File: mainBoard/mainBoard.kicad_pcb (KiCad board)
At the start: 4 copper layers, 50 x 60 mm, 46 parts, among them J1 Conn_01x04, J10 Conn_02x07_Odd_Even, J2 Conn_01x04, J3 Conn_01x03, J6 Conn_01x07, J7 Conn_01x07, J8 Conn_01x02, M1 Conn_01x01, M2 Conn_01x01, U1 MAX15062A, U2 STM32H503CBT6, U3 DRV8251ADDAR

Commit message: Popisky
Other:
- board text added: "CURRENT_SENS"
- board text added: "SERVIO_PSB V 1.0"
- board text removed: "PROUD"
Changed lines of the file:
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@@
     (effects (font (size 1.5 1.5) (thickness 0.2)) (justify left bottom mirror))
   )
-  (gr_text "PROUD" (at 135 92.5) (layer "B.SilkS")
+  (gr_text "CURRENT_SENS" (at 133.45 92.5) (layer "B.SilkS")
     (effects (font (size 1.5 1.5) (thickness 0.2)) (justify bottom mirror))
   )
@@
     (effects (font (size 1.5 1.5) (thickness 0.2)) (justify bottom))
   )
-  (gr_text "PROUD" (at 135 92.5) (layer "F.SilkS")
+  (gr_text "SERVIO_PSB V 1.0" (at 170.875 93.75 90) (layer "F.SilkS")
+    (effects (font (size 1.5 1.5) (thickness 0.3) bold) (justify left bottom))
+  )
+  (gr_text "CURRENT_SENS" (at 133.45 92.5) (layer "F.SilkS")
     (effects (font (size 1.5 1.5) (thickness 0.2)) (justify bottom))
   )

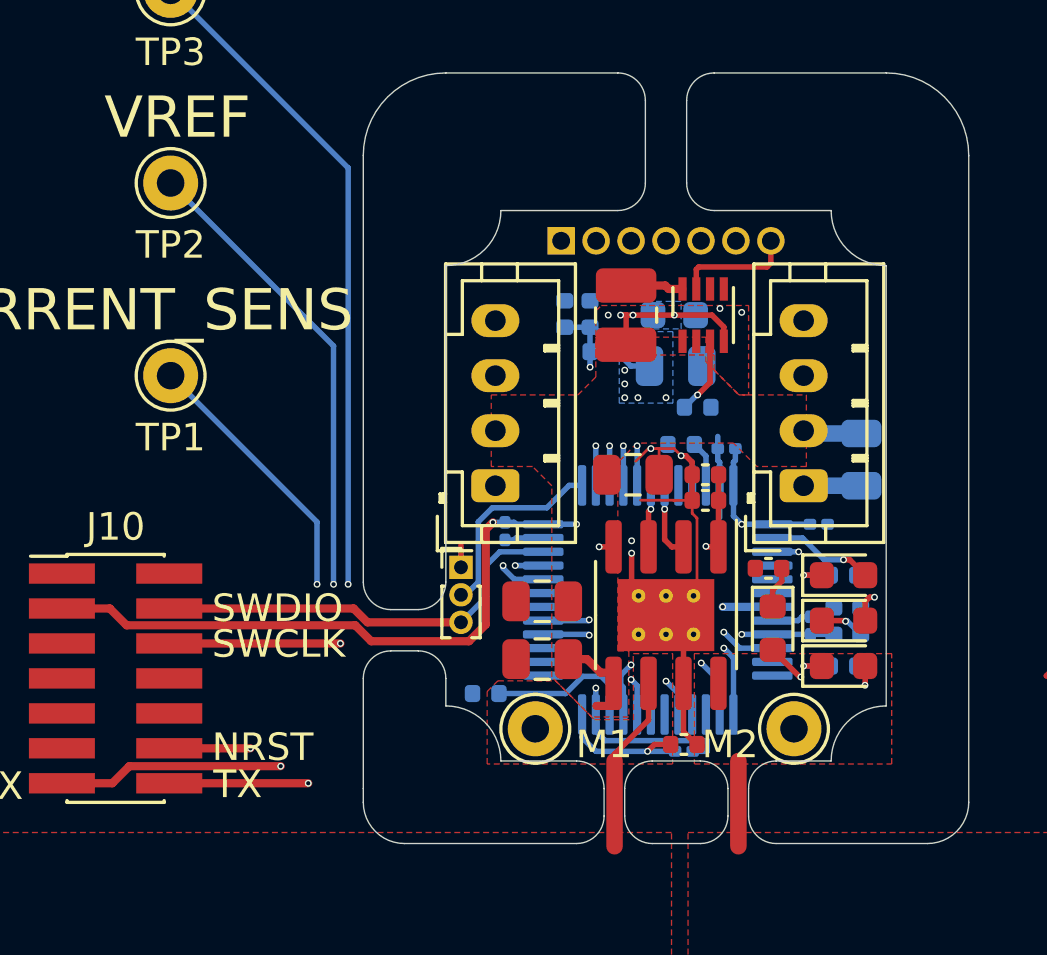
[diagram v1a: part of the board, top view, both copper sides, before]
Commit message: Větší via
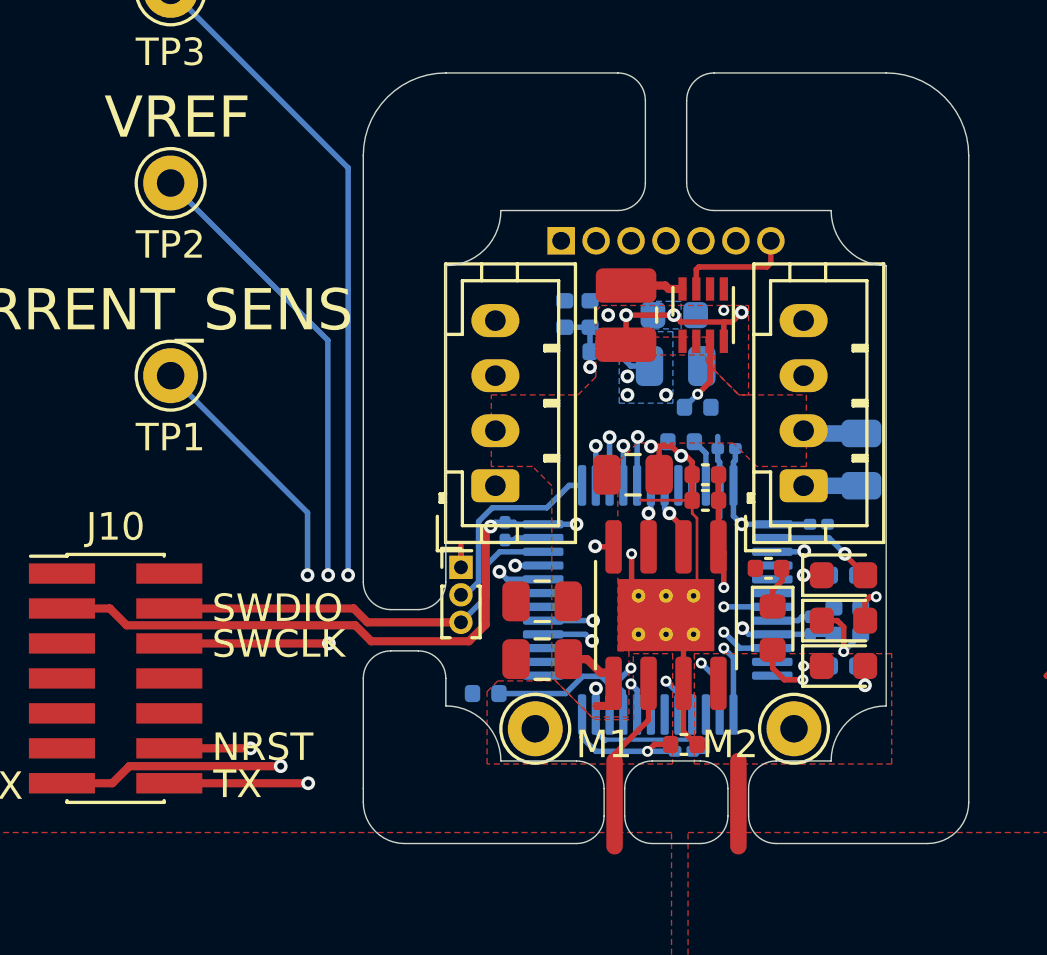
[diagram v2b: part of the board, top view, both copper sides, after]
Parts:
- moved C13 0.10 mm to (153.6, 96.4)
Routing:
- net /CPU/UART.RX: track 26.7 -> 28.3 mm
- net Net-(D3-K): track 1.62 -> 2.66 mm
- net /CPU/DRV.VREF: track 41.4 -> 42.3 mm
- net VDD: track 91.7 -> 92.6 mm, vias 10 -> 9
- net /CPU/MEŘENÍ-NAPÁJENÍ: track 53.4 -> 54.2 mm
- net /CPU/LED.Y: track 9.78 -> 10.4 mm
- net GND: track 62.6 -> 62.2 mm, vias 5 -> 4
- net VCC: vias 5 -> 3

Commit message: drobeček
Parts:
- removed D1: LED-R, LED_SMD:LED_0603_1608Metric
- removed D2: LED-G, LED_SMD:LED_0603_1608Metric
- removed D3: LED-B, LED_SMD:LED_0603_1608Metric
- removed D4: LED-Y, LED_SMD:LED_0603_1608Metric
- removed R3: 1k, Capacitor_SMD:C_0402_1005Metric
- removed TP1, TP2, TP3, TP4: Conn_01x01, Connector_Pin:Pin_D1.0mm_L10.0mm
- added D5: LED_RGAB, LED_SMD:LED_LiteOn_LTST-C19HE1WT, F.Cu at (142.6, 96.7)
- added J11: Conn_01x01, RKL-Connectors:YZ157015035P-01-contact_pad, F.Cu at (144.8, 99.1)
- added J12: Conn_01x01, RKL-Connectors:YZ157015035P-01-contact_pad, F.Cu at (142.2, 101.6)
- added J13: Conn_01x01, RKL-Connectors:YZ157015035P-01-contact_pad, F.Cu at (144.8, 101.6)
- added J4: Conn_01x01, RKL-Connectors:YZ157015035P-01-contact_pad, F.Cu at (146.2, 107.2)
- added J9: Conn_01x01, RKL-Connectors:YZ157015035P-01-contact_pad, F.Cu at (142.2, 99.1)
- added U4: 64Kbit, RKL-StandardPackages:XFBGA-6, F.Cu at (148.7, 98.2)
- C1, C3, C4: moved to F.Cu
- C14: footprint Capacitor_SMD:C_0805_2012Metric -> Capacitor_SMD:C_0603_1608Metric; moved to F.Cu
- C15, R6: footprint Capacitor_SMD:C_0402_1005Metric -> Capacitor_SMD:C_0201_0603Metric
- C16, C17: footprint Capacitor_SMD:C_0805_2012Metric -> Capacitor_SMD:C_0603_1608Metric
- C18: footprint Capacitor_SMD:C_0805_2012Metric -> Capacitor_SMD:C_0603_1608Metric; moved to B.Cu
- C2: footprint Capacitor_SMD:C_0805_2012Metric -> Capacitor_SMD:C_0402_1005Metric
- C5, L1, U1: moved to B.Cu
- J10: value Conn_02x07_Odd_Even -> Conn_01x01; footprint Connector_PinHeader_1.27mm:PinHeader_2x07_P1.27mm_Vertical_SMD -> RKL-Connectors:YZ157015035P-01-contact_pad
- J2: value Conn_01x04 -> Conn_01x01; footprint Connector_JST:JST_PH_B4B-PH-K_1x04_P2.00mm_Vertical -> RKL-Connectors:YZ157015035P-01-contact_pad
- J3: value Conn_01x03 -> Conn_01x01; footprint Connector_PinHeader_1.00mm:PinHeader_1x03_P1.00mm_Vertical -> RKL-Connectors:YZ157015035P-01-contact_pad
- J6: value Conn_01x07 -> Conn_01x01; footprint Connector_JST:JST_PH_B7B-PH-K_1x07_P2.00mm_Vertical -> RKL-Connectors:YZ157015035P-01-contact_pad
- J7: value Conn_01x07 -> Conn_01x05; footprint Connector_PinHeader_1.27mm:PinHeader_1x07_P1.27mm_Vertical -> Connector_PinHeader_2.00mm:PinHeader_1x05_P2.00mm_Vertical; moved to F.Cu
- J8: value Conn_01x02 -> Conn_01x01; footprint Connector_JST:JST_XH_B2B-XH-AM_1x02_P2.50mm_Vertical -> RKL-Connectors:YZ157015035P-01-contact_pad
- M1, M2: footprint Connector_Pin:Pin_D1.0mm_L10.0mm -> RKL-Connectors:YZ157015035P-01-contact_pad
- R1: footprint Capacitor_SMD:C_0402_1005Metric -> Resistor_SMD:R_0201_0603Metric; moved to F.Cu
- R2: footprint Capacitor_SMD:C_0402_1005Metric -> Resistor_SMD:R_0201_0603Metric
- R4, R5: footprint Capacitor_SMD:C_0402_1005Metric -> Capacitor_SMD:C_0201_0603Metric; moved to F.Cu
- R7: footprint Capacitor_SMD:C_0402_1005Metric -> Capacitor_SMD:C_0201_0603Metric; moved to B.Cu
- moved J6 26.0 mm to (147.3, 96.5)
- moved J8 24.0 mm to (149.9, 96.5), turned to 0 degrees
- moved J2 17.0 mm to (143.6, 107.2), turned to 0 degrees
- moved R4 16.8 mm to (143.2, 100.3), turned to -90 degrees
- moved J7 16.5 mm to (154.5, 104.8), turned to 180 degrees
- moved R5 16.4 mm to (143.9, 100.3), turned to -90 degrees
- moved C14 15.7 mm to (146.3, 104.5), turned to 90 degrees
- moved C1 15.7 mm to (142.0, 105.0)
- moved R2 15.6 mm to (151.9, 107.1), turned to 180 degrees
- moved C6 15.1 mm to (143.5, 98.0), turned to 90 degrees
- moved R1 14.9 mm to (144.9, 106.9), turned to -90 degrees
- moved J10 14.5 mm to (144.8, 96.5)
- moved C10 14.5 mm to (144.2, 106.6)
- moved C5 14.0 mm to (142.1, 99.5), turned to -90 degrees
- moved C7 12.1 mm to (151.4, 95.8), turned to 90 degrees
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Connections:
- J10 pad 1: unconnected-(J10-Pin_1-Pad1) -> /CPU/SWCLK
- J2 pad 1: GND -> /CPU/MEŘENÍ-NAPÁJENÍ
- J3 pad 1: GND -> /CPU/DRV.PROUD
- J6 pad 1: /CPU/ENC.POT -> /CPU/DRV.IN1
- J7 pad 1: /CPU/ENC.POT -> /CPU/ENC.CLK
- J7 pad 2: /CPU/ENC.ENC-TYP-DET -> /CPU/ENC.MISO
- J7 pad 3: /CPU/ENC.CLK -> /CPU/ENC.MOSI
- J7 pad 4: /CPU/ENC.MISO -> VDD
- J7 pad 5: /CPU/ENC.MOSI -> GND
- J8 pad 1: Net-(J8-Pin_1) -> /CPU/DRV.IN2
- M1 pad 1: Net-(J8-Pin_2) -> Net-(M1-Pin_1)
- M2 pad 1: Net-(J8-Pin_1) -> Net-(M2-Pin_1)
- R4 pad 2: GND -> /CPU/LED.G
- R5 pad 2: GND -> /CPU/LED.R
- R6 pad 2: GND -> /CPU/LED.B
- U2 pad 10: /CPU/ENC.POT -> /CPU/LED.B
- U2 pad 12: unconnected-(U2-PA2-Pad12) -> /CPU/ENC.CLK
- U2 pad 2: /CPU/LED.R -> unconnected-(U2-PC13-Pad2)
- U2 pad 20: /CPU/LED.G -> /CPU/LED.R
- U2 pad 21: /CPU/LED.Y -> /CPU/LED.G
- U2 pad 28: /CPU/UART.RX -> unconnected-(U2-PB15-Pad28)
- U2 pad 29: /CPU/UART.TX -> unconnected-(U2-PA8-Pad29)
- U2 pad 3: /CPU/LED.B -> unconnected-(U2-PC14-_OSC32_IN(OSC32_IN)-Pad3)
- U2 pad 30: unconnected-(U2-PA9-Pad30) -> /CPU/UART.TX
- U2 pad 31: unconnected-(U2-PA10-Pad31) -> /CPU/UART.RX
- U2 pad 32: /CPU/RX-1 -> /CPU/RX-2
- U2 pad 33: /CPU/TX-1 -> /CPU/TX-2
- U2 pad 38: /CPU/ENC.ENC-TYP-DET -> /CPU/EEPROM.WP
- U2 pad 39: /CPU/ENC.CLK -> /CPU/EEPROM.SCL
- U2 pad 45: unconnected-(U2-PB8-Pad45) -> /CPU/EEPROM.SDA
- U3 pad 6: Net-(J8-Pin_2) -> Net-(M1-Pin_1)
- U3 pad 8: Net-(J8-Pin_1) -> Net-(M2-Pin_1)
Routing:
- net /CPU/ENC.POT: track 45.6 -> 0.00 mm, vias 2 -> 0
- net GND: track 62.2 -> 22.9 mm, vias 4 -> 7
- net /CPU/MEŘENÍ-NAPÁJENÍ: track 54.2 -> 15.2 mm, vias 3 -> 2
- net /CPU/ENC.ENC-TYP-DET: track 30.6 -> 0.00 mm, vias 1 -> 0
- net /CPU/DRV.VREF: track 42.3 -> 15.5 mm
- net /CPU/ENC.CLK: track 29.4 -> 2.64 mm, vias 1 -> 0
- net /CPU/RX-1: track 23.1 -> 0.00 mm, vias 2 -> 0
- net /CPU/TX-1: track 19.9 -> 0.00 mm, vias 2 -> 0
- net /CPU/ENC.MOSI: track 29.7 -> 9.83 mm
- net VDD: track 92.6 -> 72.9 mm, vias 9 -> 5
- net /CPU/ENC.MISO: track 28.1 -> 10.4 mm
- net /CPU/DRV.PROUD: track 37.3 -> 20.5 mm, vias 3 -> 2
- net /CPU/SWCLK: track 18.7 -> 1.98 mm
- net /CPU/NRST: track 29.2 -> 14.5 mm, vias 2 -> 3
- net /CPU/SWDIO: track 15.5 -> 3.18 mm, vias 0 -> 1
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- added copper zone on F.Cu, net Net-(M1-Pin_1)
- added copper zone on F.Cu, net Net-(M2-Pin_1)
- added copper zone on B.Cu, net Net-(U1-LX)
- added copper zone on In2.Cu, net VCC
- added copper zone on In2.Cu, net VDD
- removed copper zone on In2.Cu, net GND
- removed copper zone on F.Cu, net Net-(J8-Pin_1)
- removed copper zone on F.Cu, net Net-(J8-Pin_2)
- removed copper zone on B.Cu, net VCC
- removed copper zone on B.Cu, net VDD
- removed copper zone on F.Cu, net VDD
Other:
- board size 50 x 60 mm -> 14 x 18 mm
- board text removed: "+"
- board text removed: "-"
- board text removed: "BAT_SENS"
- board text removed: "CLK"
- board text removed: "CURRENT_SENS"
- board text removed: "E.TYP"
- board text removed: "ENC_POT"
- board text removed: "M1"
- board text removed: "M2"
- board text removed: "MISO"
- board text removed: "MOSI"
- board text removed: "NRST"
- board text removed: "POT"
- board text removed: "RX"
- board text removed: "SERVIO_PSB V 1.0"
- board text removed: "SWCLK"
- board text removed: "SWDIO"
- board text removed: "TX"
- board text removed: "VREF"

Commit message: Wpi
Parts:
- removed the J2 at (143.6, 107.2)
- added J12: Conn_01x01, RKL-Connectors:YZ157015035P-01-contact_pad, F.Cu at (139.1, 100.4)
- added J13: Conn_01x01, RKL-Connectors:YZ157015035P-01, F.Cu at (199.8, 92.5)
- added J14: Conn_01x01, RKL-Connectors:YZ157015035P-01, F.Cu at (202.4, 90.0)
- added J15: Conn_01x01, RKL-Connectors:YZ157015035P-01, F.Cu at (202.4, 92.5)
- added J16: Conn_01x01, RKL-Connectors:YZ157015035P-01, F.Cu at (199.8, 95.1)
- added J17: Conn_01x01, RKL-Connectors:YZ157015035P-01, F.Cu at (202.4, 95.1)
- added J18: Conn_01x01, RKL-Connectors:YZ157015035P-01, F.Cu at (207.5, 90.0)
- added J19: Conn_01x01, RKL-Connectors:YZ157015035P-01, F.Cu at (204.9, 90.0)
- added J20: Conn_01x01, RKL-Connectors:YZ157015035P-01, F.Cu at (203.8, 100.6)
- added J21: Conn_01x01, RKL-Connectors:YZ157015035P-01, F.Cu at (210.0, 90.0)
- added J22: Conn_01x01, RKL-Connectors:YZ157015035P-01, F.Cu at (201.2, 100.6)
- moved C1 8.11 mm to (137.6, 92.8)
- moved C10 8.11 mm to (145.4, 87.0)
- moved C11 8.11 mm to (138.8, 97.7)
- moved C12 8.11 mm to (140.3, 97.7)
- moved C13 8.11 mm to (141.8, 97.7)
- moved C14 8.11 mm to (147.2, 91.6)
- moved C15 8.11 mm to (137.7, 86.8)
- moved C16 8.11 mm to (142.1, 86.9)
- moved C17 8.11 mm to (141.6, 91.1)
- moved C18 8.11 mm to (137.5, 98.3)
- moved C2 8.11 mm to (148.1, 91.2)
- moved C3 8.11 mm to (146.9, 89.0)
- moved C4 8.11 mm to (139.7, 99.8)
- moved C5 8.11 mm to (148.8, 96.8)
- moved C6 8.11 mm to (139.0, 91.2)
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- renumbered C5 to C1, C18 to C10, C17 to C11, C16 to C12, C14 to C13, C15 to C14, C4 to C15, C2 to C16, C3 to C17, C1 to C18, C8 to C2, C7 to C3, C10 to C4, C9 to C5, C12 to C7, C11 to C8, C13 to C9, D5 to D1, J9 to J1, J7 to J10, J1 to J11, J10 to J2, J11 to J3, J12 to J4, J13 to J5, J8 to J7, J4 to J8, J3 to J9, R7 to R1, R1 to R2, R2 to R3, R5 to R4, R4 to R5, U2 to U1, U3 to U2, U1 to U3
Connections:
- net /CPU/DRV.IN1 renamed /MotorBoard/DRV.IN1
- net /CPU/DRV.IN2 renamed /MotorBoard/DRV.IN2
- net /CPU/DRV.PROUD renamed /MotorBoard/DRV.PROUD
- net /CPU/DRV.VREF renamed /MotorBoard/DRV.VREF
- net /CPU/EEPROM.SCL renamed /MotorBoard/CPU/EEPROM.SCL
- net /CPU/EEPROM.SDA renamed /MotorBoard/CPU/EEPROM.SDA
- net /CPU/EEPROM.WP renamed /MotorBoard/CPU/EEPROM.WP
- net /CPU/ENC.CLK renamed /MotorBoard/CPU/ENC.CLK
- net /CPU/ENC.MISO renamed /MotorBoard/CPU/ENC.MISO
- net /CPU/ENC.MOSI renamed /MotorBoard/CPU/ENC.MOSI
- net /CPU/LED.B renamed /MotorBoard/CPU/LED.B
- net /CPU/LED.G renamed /MotorBoard/CPU/LED.G
- net /CPU/LED.R renamed /MotorBoard/CPU/LED.R
- net /CPU/MEŘENÍ-NAPÁJENÍ renamed /MotorBoard/CPU/MEŘENÍ-NAPÁJENÍ
- net /CPU/NRST renamed /MotorBoard/TUNING-LINES.NRST
- net /CPU/RX-2 renamed /MotorBoard/TUNING-LINES.RX-2
- net /CPU/SWCLK renamed /MotorBoard/TUNING-LINES.SWCLK
- net /CPU/SWDIO renamed /MotorBoard/TUNING-LINES.SWDIO
- net /CPU/TX-2 renamed /MotorBoard/TUNING-LINES.TX-2
- net /CPU/UART.RX renamed /MotorBoard/CPU/UART.RX
- net /CPU/UART.TX renamed /MotorBoard/CPU/UART.TX
- net VCC renamed /MotorBoard/VCC
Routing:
- net GND: track 22.9 -> 27.5 mm, vias 7 -> 9
- net /MotorBoard/CPU/MEŘENÍ-NAPÁJENÍ: track 15.2 -> 14.4 mm

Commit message: DebugBoard
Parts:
- added J23: Conn_01x05, Connector_PinHeader_2.00mm:PinHeader_1x05_P2.00mm_Vertical, F.Cu at (197.8, 76.4)
- added J24: Conn_01x04, Connector_JST:JST_PH_B4B-PH-K_1x04_P2.00mm_Vertical, F.Cu at (153.8, 55.9)
- added J25: Conn_01x05, Connector_PinHeader_2.00mm:PinHeader_1x05_P2.00mm_Vertical, F.Cu at (182.8, 76.4)
- added J26: Conn_01x05, Connector_PinHeader_2.00mm:PinHeader_1x05_P2.00mm_Vertical, F.Cu at (167.8, 76.4)
- added J27: Conn_01x05, Connector_PinHeader_2.00mm:PinHeader_1x05_P2.00mm_Vertical, F.Cu at (152.8, 76.4)
- added J28: Conn_01x04, Connector_JST:JST_PH_B4B-PH-K_1x04_P2.00mm_Vertical, F.Cu at (168.8, 55.9)
- added J29: Conn_01x04, Connector_JST:JST_PH_B4B-PH-K_1x04_P2.00mm_Vertical, F.Cu at (198.8, 55.9)
- added J30: Conn_01x04, Connector_JST:JST_PH_B4B-PH-K_1x04_P2.00mm_Vertical, F.Cu at (183.8, 55.9)
- added J31: Conn_02x05_Odd_Even, Connector_PinHeader_1.27mm:PinHeader_2x05_P1.27mm_Vertical, F.Cu at (132.4, 108.6)
- added J32: Conn_02x07_Odd_Even, Connector_PinHeader_1.27mm:PinHeader_2x07_P1.27mm_Vertical, F.Cu at (156.2, 108.6)
- added J33: Conn_01x04, Connector_PinHeader_2.54mm:PinHeader_1x04_P2.54mm_Vertical, F.Cu at (132.0, 82.6)
- added J34: Conn_01x02, Connector_PinHeader_2.54mm:PinHeader_1x02_P2.54mm_Vertical, F.Cu at (216.8, 105.2)
- added J35: Conn_01x02, Connector_PinHeader_2.54mm:PinHeader_1x02_P2.54mm_Vertical, F.Cu at (216.8, 62.7)
- added J37: Conn_01x02, Connector_PinHeader_2.54mm:PinHeader_1x02_P2.54mm_Vertical, F.Cu at (170.0, 107.7)
- added J38: Conn_01x02, Connector_PinHeader_2.54mm:PinHeader_1x02_P2.54mm_Vertical, F.Cu at (131.5, 73.9)
- moved J21 89.7 mm to (128.3, 53.0)
- moved J18 85.1 mm to (130.8, 53.0)
- moved J19 80.5 mm to (133.4, 53.0)
- moved J20 78.5 mm to (134.5, 63.6)
- moved J14 76.1 mm to (135.9, 53.0)
- moved J15 76.1 mm to (135.9, 55.5)
- moved J17 76.1 mm to (135.9, 58.1)
- moved J22 74.1 mm to (137.1, 63.6)
- moved J13 71.7 mm to (138.5, 55.5)
- moved J16 71.7 mm to (138.5, 58.1)
- moved C11 47.0 mm to (95.6, 79.1)
- moved C12 47.0 mm to (97.1, 79.1)
- moved C13 47.0 mm to (98.6, 79.1)
- moved C14 47.0 mm to (103.9, 73.0)
- moved C8 47.0 mm to (95.7, 81.1)
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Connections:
- net /MotorBoard/CPU/MEŘENÍ-NAPÁJENÍ renamed /MotorBoard/CPU/SUPPLY_VOLTAGE_MEASUREMENT
- net /MotorBoard/DRV.PROUD renamed /MotorBoard/DRV.CURRENT
- net GND renamed VSS
- J20 pad 1: /DebuBoard/DB-DRV.VREF -> /DebuBoard/DB-TUNING-LINES.TRACESWO
- J21 pad 1: /DebuBoard/DB-DRV.PROUD -> /DebuBoard/DB-DRV.CURRENT
- J22 pad 1: unconnected-(J22-Pin_1-Pad1) -> /DebuBoard/GND
- J8 pad 1: /MotorBoard/DRV.VREF -> /MotorBoard/TUNING-LINES.TRACESWO
- U1 pad 10: /MotorBoard/CPU/LED.B -> /MotorBoard/CPU/LED.R
- U1 pad 11: unconnected-(U1-PA1-Pad11) -> /MotorBoard/CPU/LED.B
- U1 pad 12: /MotorBoard/CPU/ENC.CLK -> /MotorBoard/CPU/LED.G
- U1 pad 20: /MotorBoard/CPU/LED.R -> unconnected-(U1-PB2-Pad20)
- U1 pad 21: /MotorBoard/CPU/LED.G -> /MotorBoard/CPU/EEPROM.SCL
- U1 pad 26: unconnected-(U1-PB13-Pad26) -> /MotorBoard/CPU/EEPROM.SDA
- U1 pad 29: unconnected-(U1-PA8-Pad29) -> /MotorBoard/CPU/ENC.CLK
- U1 pad 39: /MotorBoard/CPU/EEPROM.SCL -> /MotorBoard/TUNING-LINES.TRACESWO
- U1 pad 45: /MotorBoard/CPU/EEPROM.SDA -> unconnected-(U1-PB8-Pad45)
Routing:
- net /DebuBoard/DB-TUNING-LINES.RX-2: track 0.00 -> 87.9 mm, vias 0 -> 1
- net /DebuBoard/DB-TUNING-LINES.SWCLK: track 0.00 -> 86.1 mm, vias 0 -> 1
- net /DebuBoard/DB-TUNING-LINES.NRST: track 0.00 -> 85.5 mm, vias 0 -> 1
- net /DebuBoard/DB-TUNING-LINES.SWDIO: track 0.00 -> 83.7 mm, vias 0 -> 2
- net /DebuBoard/DB-TUNING-LINES.TX-2: track 0.00 -> 81.1 mm, vias 0 -> 1
- net /DebuBoard/ENC.MOSI: track 0.00 -> 57.1 mm, vias 0 -> 3
- net /DebuBoard/ENC.CLK: track 0.00 -> 55.4 mm, vias 0 -> 3
- net /DebuBoard/3V3: track 0.00 -> 53.1 mm
- net Net-(J24-Pin_2): track 0.00 -> 53.0 mm
- net /DebuBoard/ENC.MISO: track 0.00 -> 52.6 mm
- net /DebuBoard/DB-TUNING-LINES.TRACESWO: track 0.00 -> 50.0 mm
- net /DebuBoard/UART.RX: track 0.00 -> 49.5 mm
- net /DebuBoard/UART.TX: track 0.00 -> 49.5 mm
- net /DebuBoard/DB-DRV.CURRENT: track 0.00 -> 36.2 mm
- net /DebuBoard/DB-DRV.IN2: track 0.00 -> 34.2 mm
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- added copper zone on B.Cu, net /DebuBoard/GND
- added copper zone on F.Cu, net /DebuBoard/GND
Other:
- board size 14 x 18 mm -> 128.2 x 64.5 mm
- board text added: "3V3"
- board text added: "CLK"
- board text added: "CURRENT"
- board text added: "DRV.IN1"
- board text added: "DRV.IN2"
- board text added: "GND"
- board text added: "MISO"
- board text added: "MOSI"
- board text added: "NRST"
- board text added: "RX"
- board text added: "RX-2"
- board text added: "SWCLK"
- board text added: "SWDIO"
- board text added: "Servio DebugBoard V1.0.0"
- board text added: "TRACESWO"
- board text added: "TX"
- board text added: "TX-2"
- board text added: "VCC (4.5-20V)"

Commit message: Add power LEDs and UART connector
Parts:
- added D2: LED, LED_SMD:LED_0603_1608Metric, F.Cu at (149.5, 56.0)
- added D3: LED, LED_SMD:LED_0603_1608Metric, F.Cu at (176.0, 99.5)
- added D4: LED, LED_SMD:LED_0603_1608Metric, F.Cu at (173.5, 99.5)
- added J36: Conn_01x03, Connector_PinHeader_2.54mm:PinHeader_1x03_P2.54mm_Vertical, F.Cu at (173.5, 108.0)
- added R7: 2k, Capacitor_SMD:C_0603_1608Metric, F.Cu at (149.5, 60.5)
- added R8: 1k, Capacitor_SMD:C_0603_1608Metric, F.Cu at (173.5, 103.5)
- added R9: 1k, Capacitor_SMD:C_0603_1608Metric, F.Cu at (176.0, 103.5)
- moved J37 20.2 mm to (190.0, 105.2), turned to 0 degrees
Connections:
- net VSS renamed GND
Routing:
- net /DebuBoard/3V3: track 53.1 -> 79.1 mm, vias 0 -> 1
- net /DebuBoard/DB-TUNING-LINES.TX-2: track 81.1 -> 98.4 mm
- net /DebuBoard/DB-TUNING-LINES.RX-2: track 87.9 -> 100.5 mm
- net Net-(D2-A): track 53.0 -> 60.2 mm
- net Net-(D2-K): track 0.00 -> 2.94 mm
- net Net-(D4-A): track 0.00 -> 2.44 mm
- net Net-(D3-A): track 0.00 -> 2.44 mm
